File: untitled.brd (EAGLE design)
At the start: 76.2 x 50.8 mm, 48 parts, among them IC1 NINA-B306-00B, IC2 INA126E, IC3 MCP6001T_SOT23, IC4 MAX8559ETAAA+T, J1 USB4105-GF-A, J2 1761681-7, J3 DM3CS-SF-PEJMS, Q1 NTR5103NT1G, Q2 NTR5103NT1G, T1+ TESTPOINT_TPS-SMD-10SN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

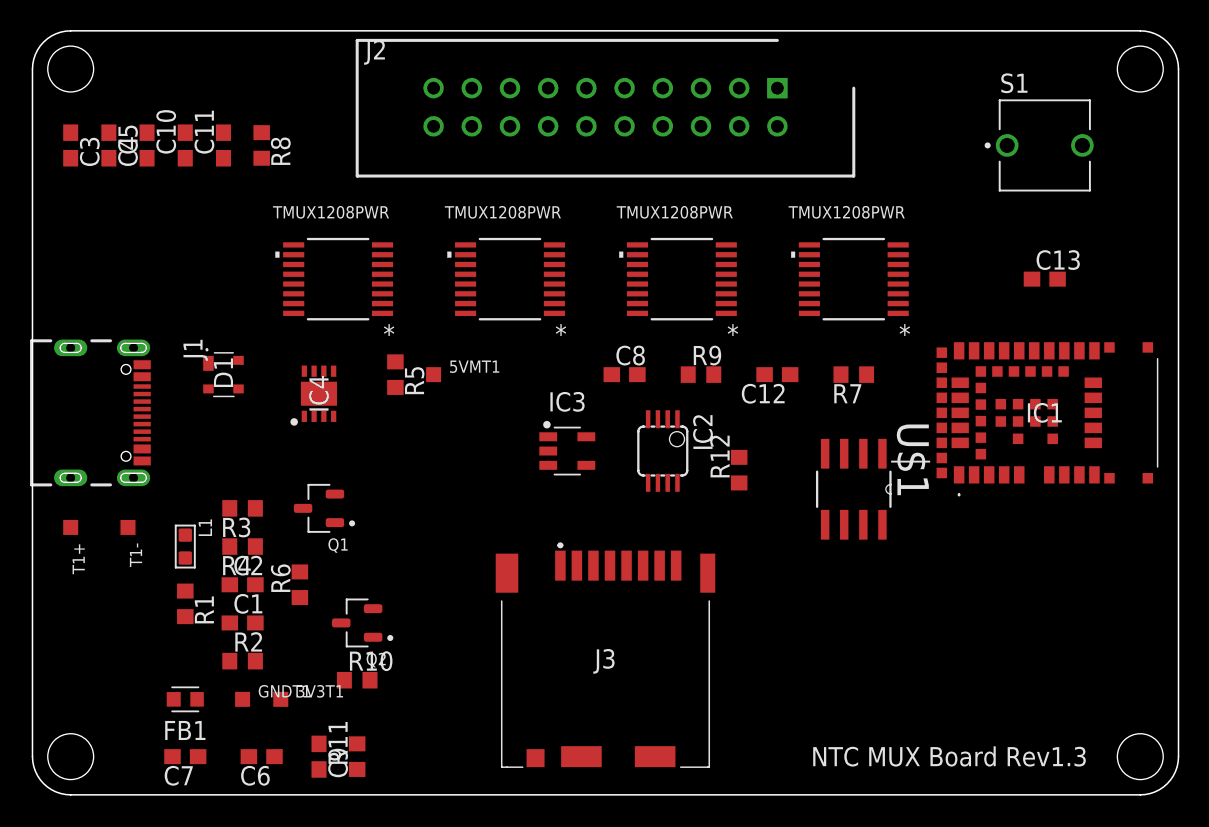
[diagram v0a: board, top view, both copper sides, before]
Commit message: lista actualizada de pendientes
faltan algunas cosas, pero la base ya está para solo unir y rutear
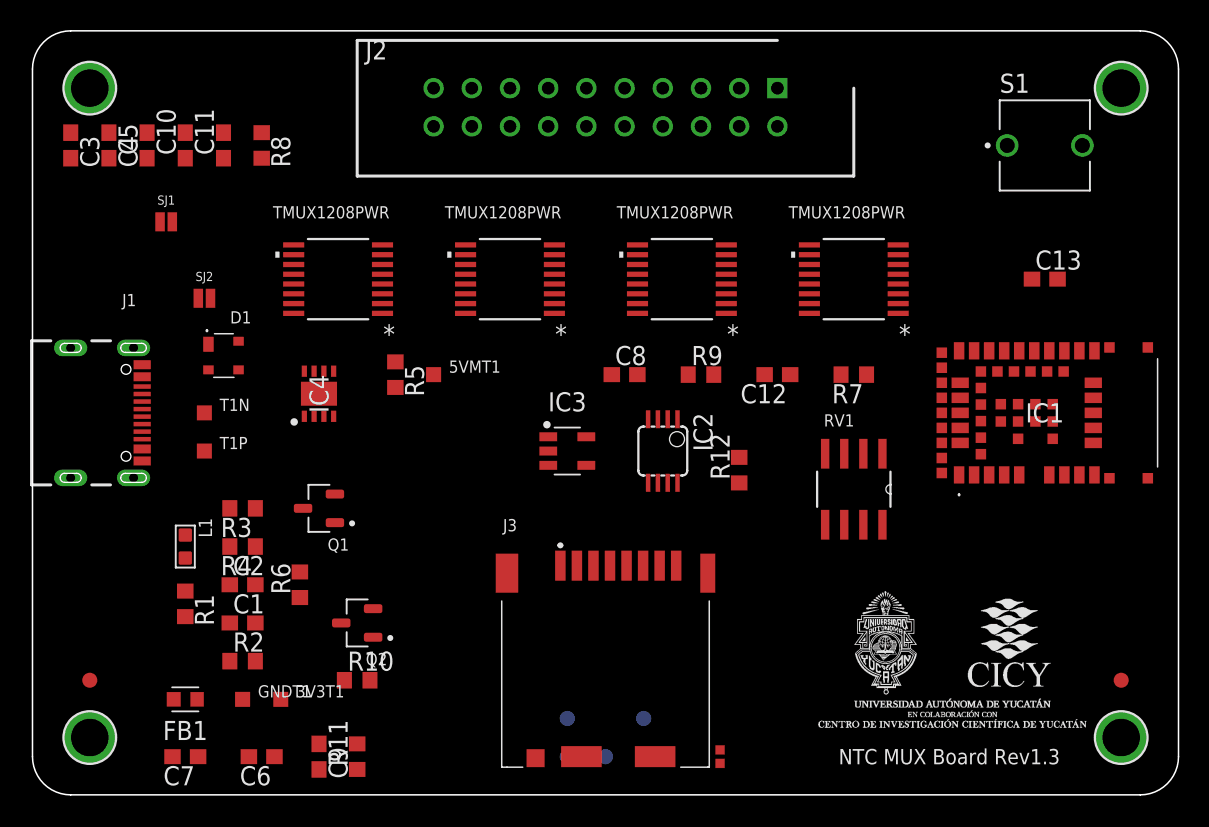
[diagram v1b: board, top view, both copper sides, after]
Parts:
- removed T1+, T1-: TESTPOINT_TPS-SMD-10SN, 52101-101-REV-A_v16:TESTPOINT_SMD-10SN
- added FID1, FID4: FIDUCIAL_1MM, microbuilder:FIDUCIAL_1MM
- added J4: DNP, Arduino-connectors:2X03-TP1
- added R13: DNP, Arduino-rcl:0402-1005X55N
- added SJ1, SJ2: JUMPER-SMT_2_NO_NO-SILK, SparkFun-Jumpers:SMT-JUMPER_2_NO_NO-SILK
- added T1N, T1P: TESTPOINT_TPS-SMD-10SN, 52101-101-REV-A_v16:TESTPOINT_SMD-10SN
- added U$2, U$24, U$3, U$4: MOUNTINGHOLE2.5, microbuilder:MOUNTINGHOLE_2.5_PLATED
- added U$5: (no value), UADY-CICY:UADY-CICY-MID
- moved D1 1.27 mm to (12.7, 29.2)
- renumbered U$1 to RV1
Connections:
- new net +3V3: J4.1, R13.1
- new net RESETN: J4.6
- new net SWCLK: J4.3, R13.2
- new net SWDIO: J4.2
- new net USB_N: SJ2.2
- new net USB_P: SJ1.2
- net GND: now also J4.5
- net USB+: now also SJ1.1, T1P.TP; no longer T1+.TP
- net USB-: now also SJ2.1, T1N.TP; no longer T1-.TP
